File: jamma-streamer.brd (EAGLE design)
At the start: 180.3 x 92 mm, 49 parts, among them IC1 LM7805, J1 Audio line out, J2 ICSP, J3 SDCARD, J4 USB, T1 TY-145P, T2 TY-145P, U1 CD74HC165MD16-M, U2 ATMEGA328PB-AUR, U3 74HC4050D, U4 TLV757X / LP298X, U5 CD74HC165MD16-M, U6 CD74HC165MD16-M, U7 FT232RL, Y1 16MHz

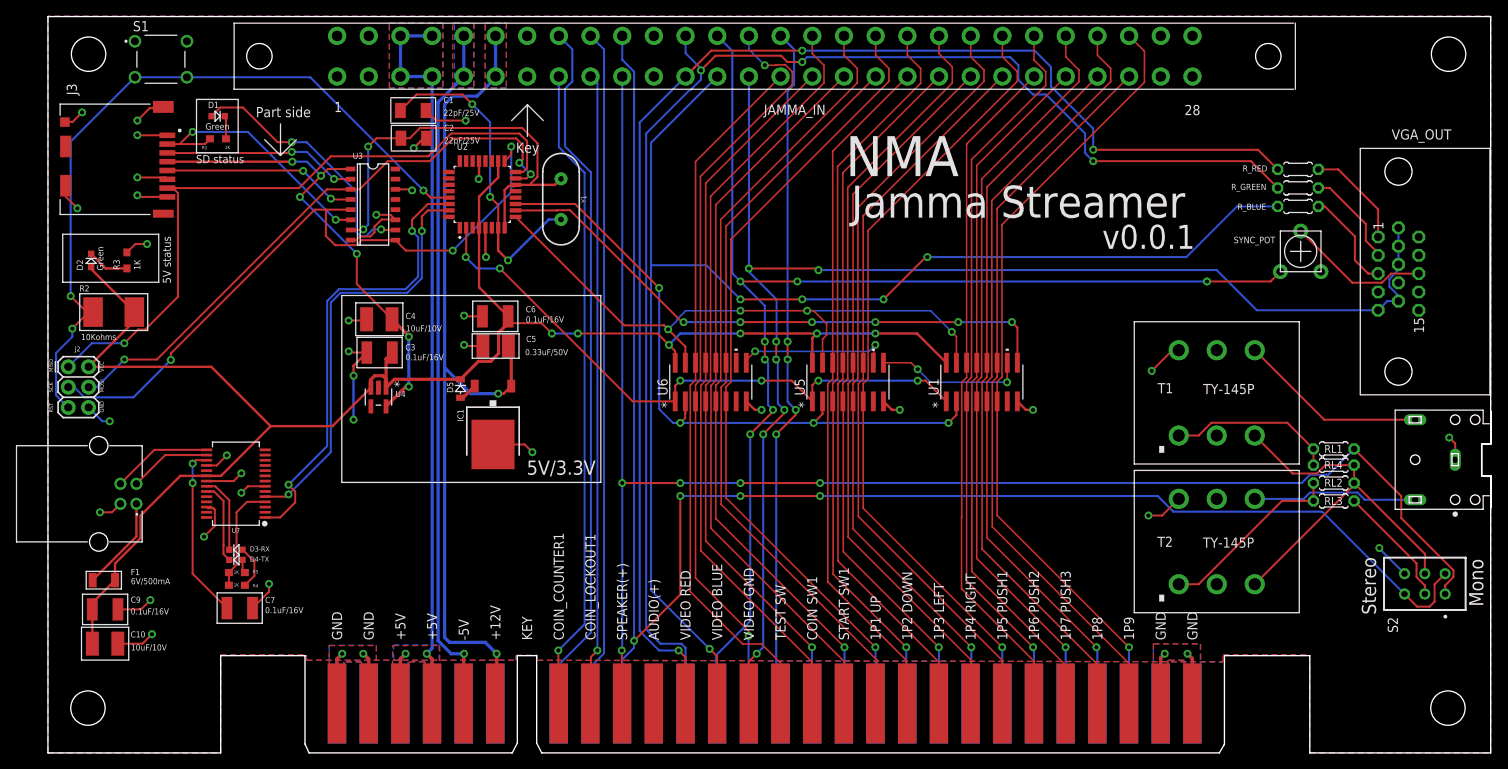
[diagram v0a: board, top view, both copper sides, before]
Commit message: New version including RTC and better alim
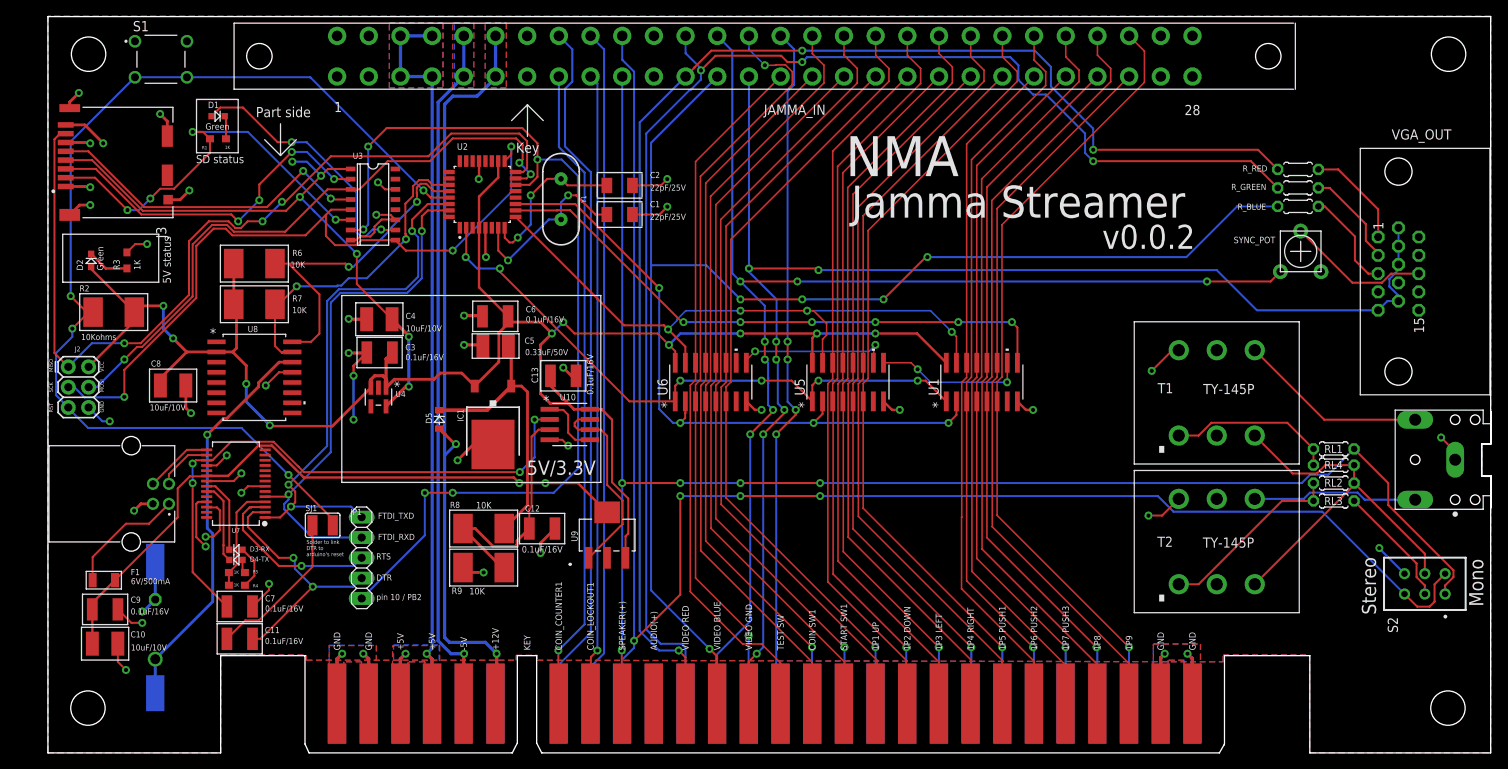
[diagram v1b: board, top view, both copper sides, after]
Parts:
- added B1: S8411-45R, S8411R:S8411-45R
- added C11, C12, C13: 0.1uF/16V, CMS:KEMET-C1210C104K4J
- added C8: 10uF/10V, CMS:KEMET-C1210C106K8N
- added JP1: (no value), pinhead:1X05
- added R6, R7, R8, R9: 10K, CMS:BOURNS-CRM2512AJW-103ELF
- added SJ1: (no value), jumper:SJW
- added U10: LM358DTD8-M, LM358D:D8-M
- added U8: DS3231SNT&R21-0042B_16-M, DS3231:21-0042B_16-M
- added U9: NDT2955SOT-223-M, NDT2955:SOT-223-M
- moved C1 28.9 mm to (71.5, 67.3)
- moved C2 26.4 mm to (71.5, 70.9)
- moved D5 4.68 mm to (48.9, 41.7)
- moved J4 4.06 mm to (10.4, 32.4)
- moved C7 0.20 mm to (24.0, 18.3)
- turned J3 to 270 degrees
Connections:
- net N$13 renamed PB6
- removed net N$11: C7.2, U7.17
- new net CMD_GATE: U10.6, U10.7, U9.1
- new net CMP: C12.1, R8.1, R9.2, U10.3
- new net DTR: C11.1, JP1.4, U7.2
- new net N$13: C11.2, SJ1.1
- new net N$31: B1.1, B1.2, U8.14
- new net PB7: C2.1, U2.8, Y1.1
- new net RTS: JP1.3, U7.3
- new net SCL: R6.2, U2.28, U8.16
- new net SDA: R7.2, U2.27, U8.15
- new net USBVCC: C10.1, C9.1, F1.2, U7.20, U9.4
- new net VCC33: C7.2, U10.2, U7.17
- new net VIN: C5.1, D5.1, IC1.1, R8.2
- net CS: now also JP1.5; no longer C2.1, U2.8, Y1.1
- net FTDI_RXD: now also JP1.2
- net FTDI_TXD: now also JP1.1
- net GND: now also B1.3, B1.4, C12.2, C13.2, C8.2, R9.1, U10.4, U8.13
- net JAMMA+12V: now also D5.2; no longer C5.1, IC1.1
- net N$23: now also U10.1, U10.5; no longer D5.2, IC1.2
- net RESET: now also SJ1.2
- net VCC: now also C13.1, C8.1, IC1.2, R6.1, R7.1, U10.8, U8.2, U9.3; no longer C10.1, C9.1, D5.1, F1.2, U7.20
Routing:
- net USBVCC: track 0.00 -> 83.2 mm, vias 0 -> 2
- net VCC33: track 0.00 -> 72.5 mm, vias 0 -> 4
- net CS: track 53.0 -> 121.9 mm, vias 2 -> 5
- net N$31: track 0.00 -> 50.2 mm, vias 0 -> 1
- net SCL: track 0.00 -> 41.9 mm, vias 0 -> 2
- net RESET: track 94.6 -> 134.2 mm, vias 3 -> 4
- net SDA: track 0.00 -> 39.6 mm, vias 0 -> 2
- net GND: track 185.0 -> 221.8 mm, vias 40 -> 49
- net VIN: track 0.00 -> 36.0 mm
- net DTR: track 0.00 -> 32.3 mm, vias 0 -> 2
- net CMP: track 0.00 -> 31.8 mm
- net DO: track 84.3 -> 110.3 mm, vias 1 -> 3
- net CMD_GATE: track 0.00 -> 24.9 mm
- net VCC: track 213.2 -> 237.2 mm, vias 6 -> 10
- net RTS: track 0.00 -> 22.3 mm, vias 0 -> 1
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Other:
- board text added: "DTR"
- board text added: "FTDI_RXD"
- board text added: "FTDI_TXD"
- board text added: "RTS"
- board text added: "Solder to link DTR to arduino's reset"
- board text added: "pin 10 / PB2"
- board text added: "v0.0.2"
- board text removed: "v0.0.1"

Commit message: Updating readme with more info
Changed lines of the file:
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@@
 <?xml version="1.0" encoding="utf-8"?>
 <!DOCTYPE eagle SYSTEM "eagle.dtd">
-<eagle version="9.2.2">
+<eagle version="9.6.2">
 <drawing>
 <settings>
@@
 <wire x1="36.73" y1="33.81" x2="36.73" y2="57.175" width="0.1524" layer="21"/>
 <text x="59.84875" y="34.76625" size="1.778" layer="21">5V/3.3V</text>
-<text x="6.985" y="47.625" size="0.508" layer="21" rot="R90">VCC</text>
-<text x="6.985" y="42.545" size="0.508" layer="21" rot="R90">GND</text>
-<text x="0.635" y="47.625" size="0.508" layer="21" rot="R90">MISO</text>
-<text x="0.635" y="45.085" size="0.508" layer="21" rot="R90">SCK</text>
-<text x="0.635" y="42.545" size="0.508" layer="21" rot="R90">RST</text>
-<text x="6.985" y="45.085" size="0.508" layer="21" rot="R90">MOSI</text>
+<text x="7.3914" y="47.625" size="0.8128" layer="21" rot="R90">VCC</text>
+<text x="7.3914" y="41.529" size="0.8128" layer="21" rot="R90">GND</text>
+<text x="1.0414" y="47.2186" size="0.8128" layer="21" rot="R90">MISO</text>
+<text x="1.0414" y="44.4754" size="0.8128" layer="21" rot="R90">SCK</text>
+<text x="1.0414" y="41.529" size="0.8128" layer="21" rot="R90">RST</text>
+<text x="7.3914" y="44.4754" size="0.8128" layer="21" rot="R90">MOSI</text>
 <polygon width="0.1524" layer="39">
 <vertex x="32.385" y="11.6078"/>
@@
 <text x="41.0464" y="24.1808" size="0.762" layer="25">RTS</text>
 <text x="41.0464" y="21.5392" size="0.762" layer="25">DTR</text>
-<text x="32.3088" y="24.5872" size="0.508" layer="25">Solder to link
+<text x="30.6832" y="23.368" size="0.762" layer="25">Solder to link
 DTR to
 arduino's reset</text>
@@
 <attribute name="MF" value="Hirose" x="6.57125" y="90" size="1.778" layer="27" rot="R270" display="off"/>
 <attribute name="MP" value="DM3CS-SF" x="6.57125" y="90" size="1.778" layer="27" rot="R270" display="off"/>
-<attribute name="NAME" x="13.523209375" y="65.78796875" size="1.27506875" layer="25" rot="R270"/>
+<attribute name="NAME" x="16.164809375" y="67.81996875" size="1.27506875" layer="25" rot="R270"/>
 <attribute name="PACKAGE" value="None" x="6.57125" y="90" size="1.778" layer="27" rot="R270" display="off"/>
-<attribute name="VALUE" x="15.684259375" y="82.13508125" size="1.27478125" layer="27" rot="R180"/>
+<attribute name="VALUE" x="12.026659375" y="82.94788125" size="1.27478125" layer="27" rot="R180"/>
 </element>
 <element name="U3" library="74HC4050D" package="SO16" value="74HC4050D" x="40.635" y="68.54" smashed="yes" rot="R270">
@@
 <attribute name="MF" value="Toshiba Semiconductor" x="40.635" y="68.54" size="1.778" layer="27" rot="R270" display="off"/>
 <attribute name="MP" value="74HC4050D" x="40.635" y="68.54" size="1.778" layer="27" rot="R270" display="off"/>
-<attribute name="NAME" x="38.09433125" y="74.256509375" size="0.762" layer="25" ratio="10"/>
+<attribute name="NAME" x="38.09433125" y="73.850109375" size="0.762" layer="25" ratio="10"/>
 <attribute name="PACKAGE" value="SOIC-16 Toshiba" x="40.635" y="68.54" size="1.778" layer="27" rot="R270" display="off"/>
 <attribute name="PRICE" value="None" x="40.635" y="68.54" size="1.778" layer="27" rot="R270" display="off"/>
@@
 </element>
 <element name="Y1" library="SparkFun-Clocks" library_urn="urn:adsk.eagle:library:511" package="HC49US" package3d_urn="urn:adsk.eagle:package:37515/1" value="16MHz" x="64.135" y="69.21875" smashed="yes" rot="R270">
-<attribute name="NAME" x="66.675" y="69.21875" size="0.6096" layer="25" font="vector" ratio="20" rot="R270" align="bottom-center"/>
+<attribute name="NAME" x="66.675" y="69.21875" size="0.762" layer="25" font="vector" rot="R270" align="bottom-center"/>
 <attribute name="PROD_ID" value="XTAL-08181" x="64.135" y="69.21875" size="1.778" layer="27" rot="R270" display="off"/>
 <attribute name="SF_ID" value="COM-00536" x="64.135" y="69.21875" size="1.778" layer="27" rot="R270" display="off"/>
-<attribute name="VALUE" x="61.595" y="69.21875" size="0.6096" layer="27" font="vector" ratio="20" rot="R270" align="top-center"/>
+<attribute name="VALUE" x="61.595" y="69.21875" size="0.762" layer="27" font="vector" rot="R270" align="top-center"/>
 </element>
 <element name="C1" library="CMS" package="KEMET-C1206C334M5RAC" value="22pF/25V" x="71.4664" y="67.2952" smashed="yes">
@@
 <attribute name="MF" value="TE Connectivity" x="14.12375" y="86.70375" size="1.778" layer="27" display="off"/>
 <attribute name="MP" value="1825910-7" x="14.12375" y="86.70375" size="1.778" layer="27" display="off"/>
-<attribute name="NAME" x="10.6194" y="90.2081" size="1.27158125" layer="25"/>
+<attribute name="NAME" x="9.6034" y="83.9089" size="1.27158125" layer="25" rot="R90"/>
 <attribute name="PACKAGE" value="None" x="14.12375" y="86.70375" size="1.778" layer="27" display="off"/>
 <attribute name="TE_PURCHASE_URL" value="https://www.te.com/usa-en/product-1825910-7.html?te_bu=Cor&amp;te_type=disp&amp;te_campaign=seda_glo_cor-seda-global-disp-prtnr-fy19-seda-model-bom-cta_sma-317_1&amp;elqCampaignId=32493" x="14.12375" y="86.70375" size="1.778" layer="27" display="off"/>
-<attribute name="VALUE" x="10.621559375" y="81.95078125" size="1.270790625" layer="27"/>
+<attribute name="VALUE" x="9.808759375" y="90.07878125" size="1.270790625" layer="27"/>
 </element>
 <element name="J2" library="SparkFun-Connectors" library_urn="urn:adsk.eagle:library:513" package="2X3" package3d_urn="urn:adsk.eagle:package:38016/1" value="ICSP" x="2.54" y="48.26" smashed="yes" rot="R270">
 <attribute name="NAME" x="4.064" y="50.8" size="0.6096" layer="25" font="vector" ratio="20" rot="R180"/>
 <attribute name="PROD_ID" value="CONN-09701" x="2.54" y="48.26" size="5.08" layer="27" rot="R270" display="off"/>
-<attribute name="VALUE" x="4.8895" y="41.275" size="0.762" layer="27" font="vector" ratio="20" rot="R180"/>
+<attribute name="VALUE" x="4.8895" y="41.275" size="0.762" layer="27" font="vector" rot="R180"/>
 </element>
 <element name="U1" library="CD74HC165M" package="D16-M" value="CD74HC165MD16-M" x="116.7384" y="46.355" smashed="yes" rot="R90">
@@
 </element>
 <element name="U7" library="SparkFun-IC-Comms" library_urn="urn:adsk.eagle:library:521" package="SSOP28DB" package3d_urn="urn:adsk.eagle:package:38718/1" value="FT232RL" x="23.495" y="33.655" smashed="yes" rot="R90">
-<attribute name="NAME" x="23.495" y="28.09875" size="0.6096" layer="25" font="vector" ratio="20" rot="R180" align="bottom-center"/>
+<attribute name="NAME" x="23.495" y="28.09875" size="0.762" layer="25" font="vector" rot="R180" align="bottom-center"/>
 <attribute name="PROD_ID" value="IC-00870" x="23.495" y="33.655" size="1.778" layer="27" rot="R90" display="off"/>
-<attribute name="VALUE" x="23.495" y="39.84625" size="0.6096" layer="27" font="vector" ratio="20" rot="R180" align="bottom-center"/>
+<attribute name="VALUE" x="23.495" y="40.04945" size="0.8128" layer="27" font="vector" rot="R180" align="bottom-center"/>
 </element>
 <element name="C7" library="CMS" package="KEMET-C1210C104K4J" value="0.1uF/16V" x="23.97125" y="18.3007" smashed="yes" rot="R180">
@@
 </element>
 <element name="R4" library="CMS" package="652-CHP0603FX1001ELF" value="1K" x="23.622" y="20.955" smashed="yes" rot="R180">
-<attribute name="NAME" x="25.61575" y="20.69" size="0.4064" layer="21"/>
+<attribute name="NAME" x="25.61575" y="20.69" size="0.6096" layer="21"/>
 <attribute name="VALUE" x="23.8695" y="21.2025" size="0.4064" layer="21" rot="R180"/>
 </element>
@@
 </element>
 <element name="R5" library="CMS" package="652-CHP0603FX1001ELF" value="1K" x="23.622" y="22.5425" smashed="yes" rot="R180">
-<attribute name="NAME" x="25.61575" y="22.43625" size="0.4064" layer="21"/>
+<attribute name="NAME" x="25.61575" y="22.43625" size="0.6096" layer="21"/>
 <attribute name="VALUE" x="23.8695" y="22.79" size="0.4064" layer="21" rot="R180"/>
 </element>

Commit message: New README, new schematic after burn fixing
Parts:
- SJ1: device jumper:SJW -> jumper:SJ
- moved SJ1 0.91 mm to (33.9, 29.3)
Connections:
- removed net VCCIO: R4.2, R5.2, U7.4
- net USBVCC: now also R4.2, R5.2, U7.4
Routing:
- net USBVCC: track 83.2 -> 104.7 mm
- net VCCIO: track 13.6 -> 0.00 mm
- net N$13: track 19.6 -> 21.7 mm, vias 0 -> 2
- net RESET: track 134.2 -> 133.0 mm
- net DTR: track 32.3 -> 32.9 mm

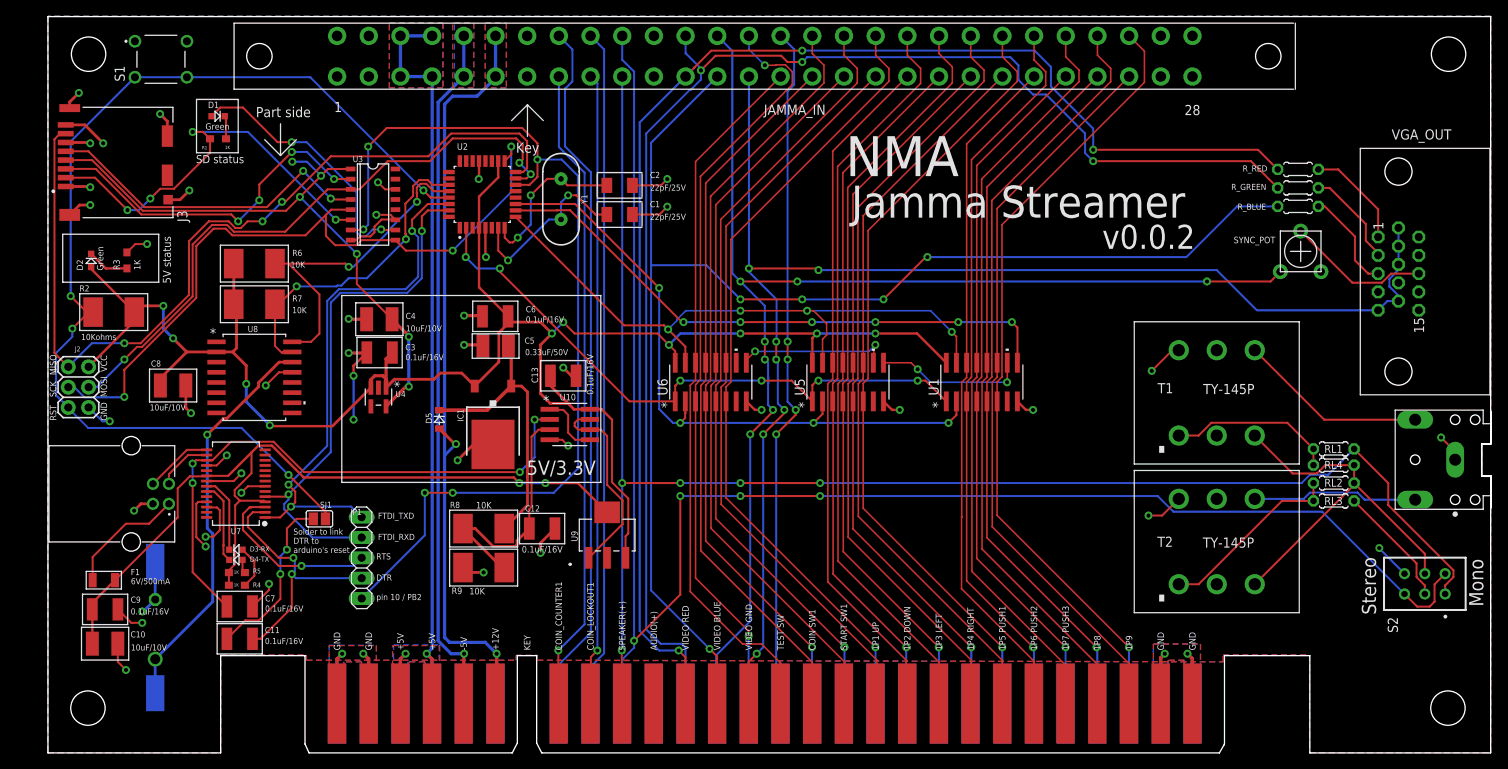
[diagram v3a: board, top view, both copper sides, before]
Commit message: Added buttons detection atmega code
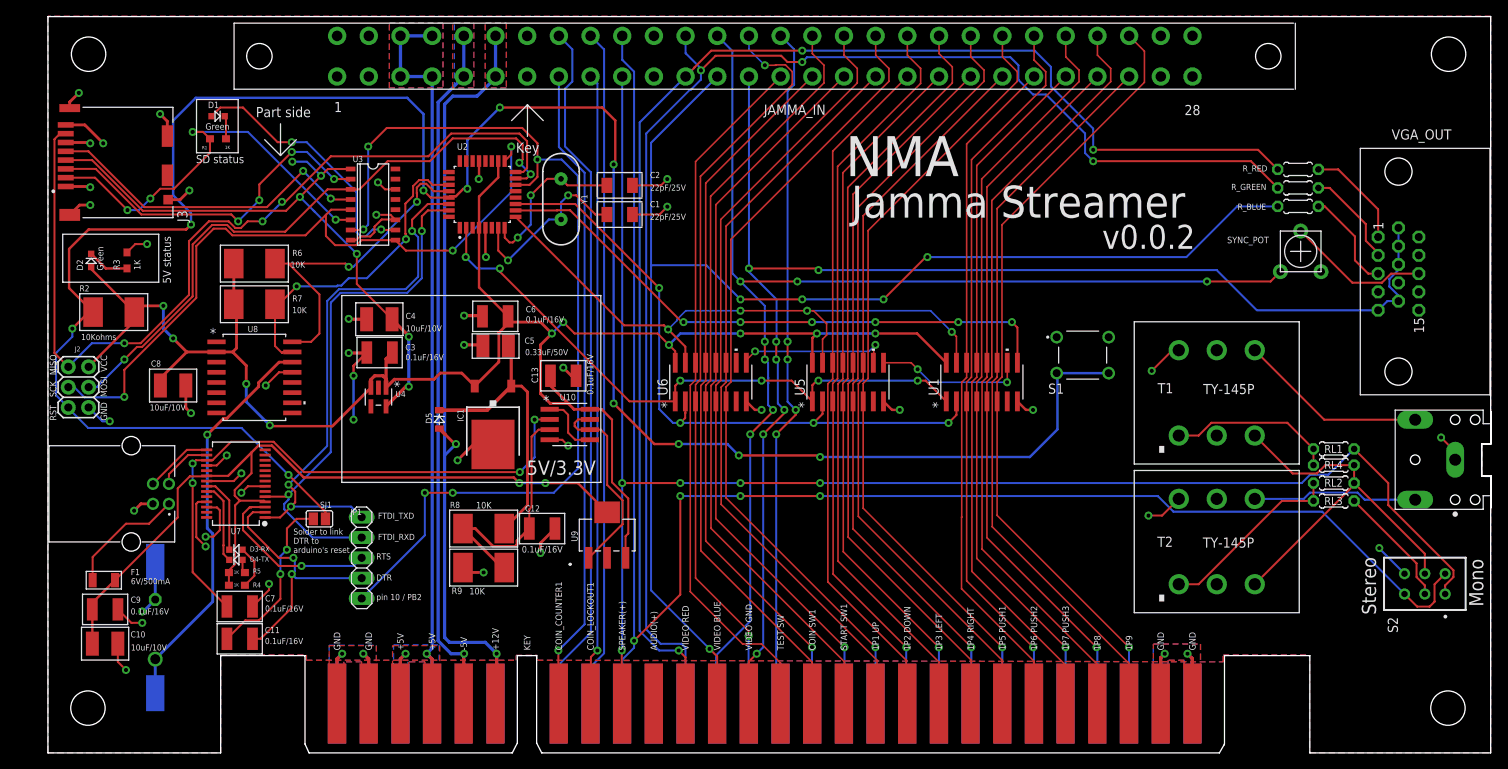
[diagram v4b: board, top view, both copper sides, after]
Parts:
- moved S1 121.0 mm to (129.3, 49.7)
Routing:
- net RESET: track 133.0 -> 277.6 mm, vias 4 -> 11
